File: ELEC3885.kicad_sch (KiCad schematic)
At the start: 4 parts

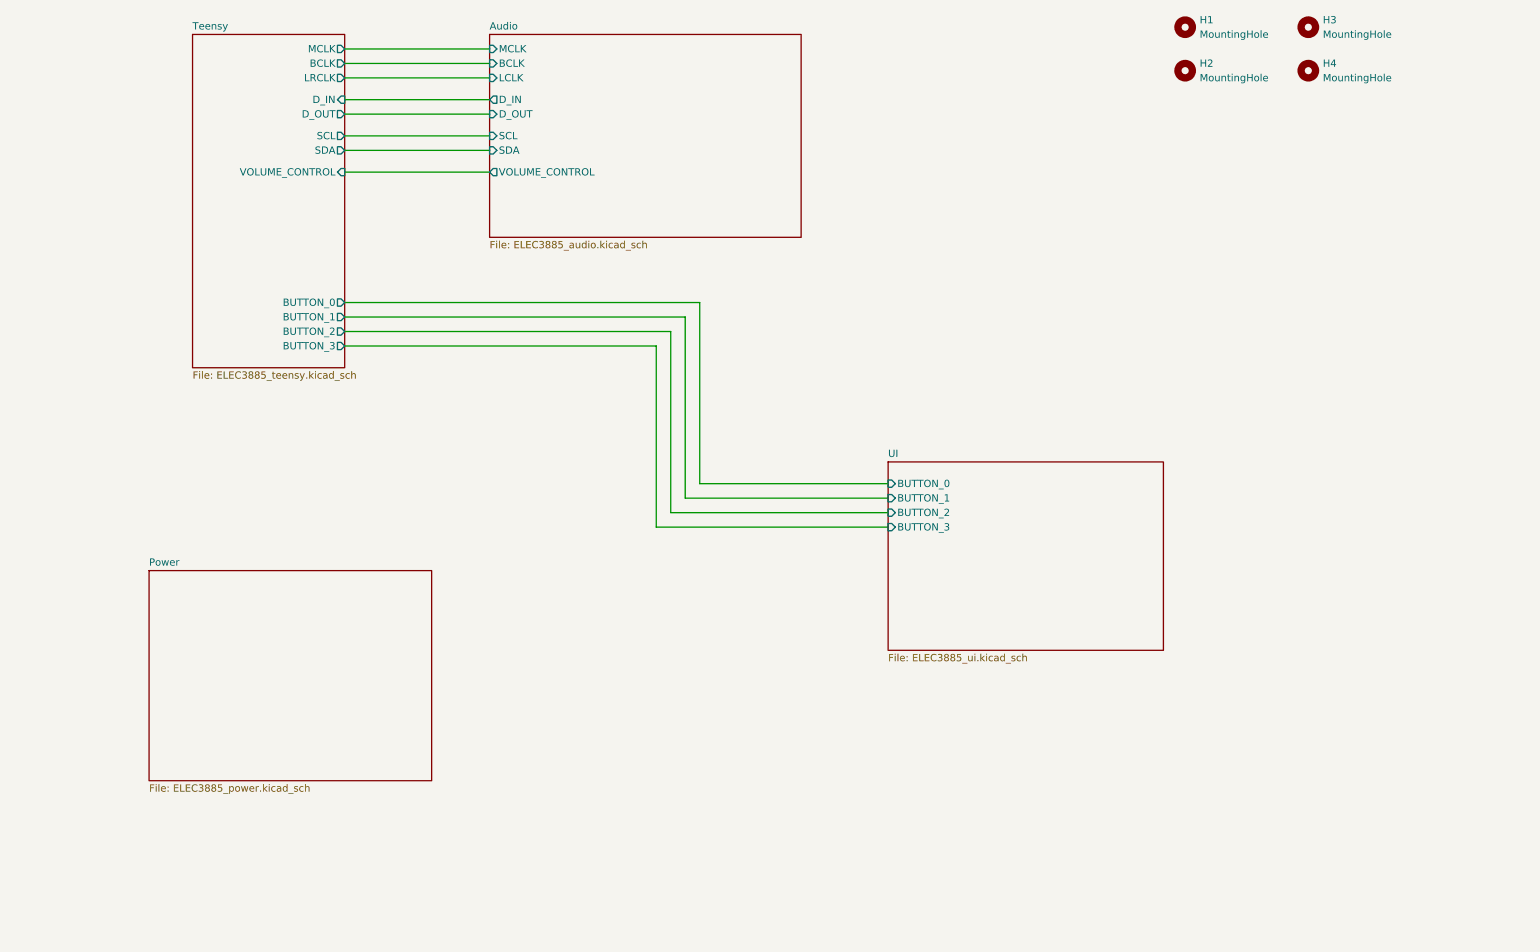
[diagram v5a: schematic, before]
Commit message: Fab cleanup, trace tapers added
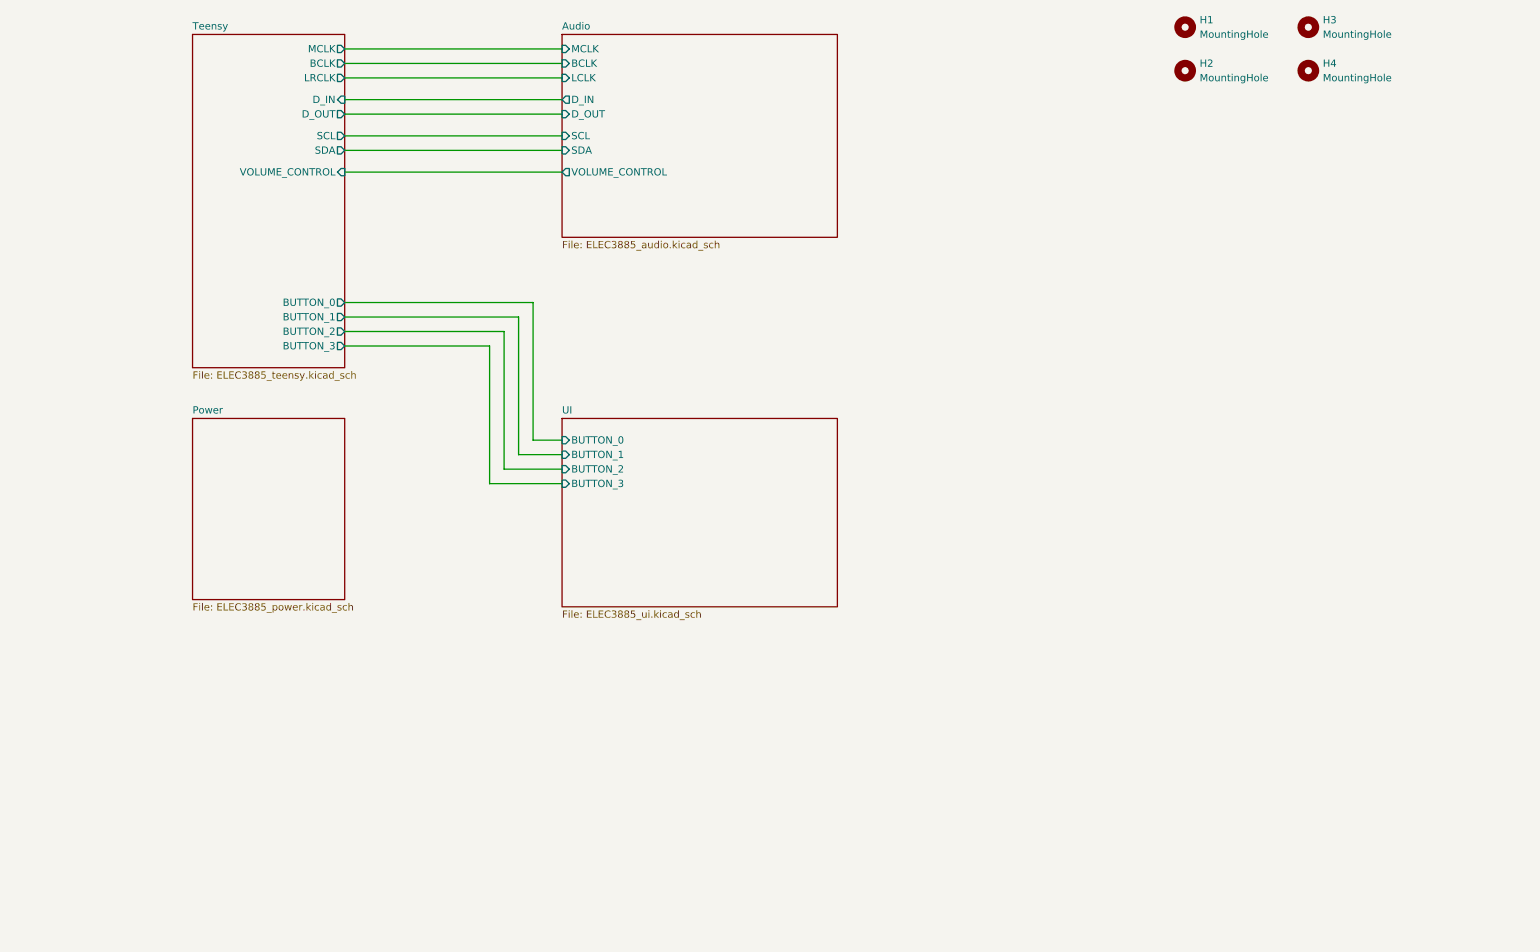
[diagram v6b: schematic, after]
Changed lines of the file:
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@@
 (kicad_sch (version 20211123) (generator eeschema)
   (paper "A4")
-  (wire (pts (xy 77.47 36.83) (xy 102.87 36.83))
-    (stroke (width 0) (type default) (color 0 0 0 0))
-  )
-  (wire (pts (xy 132.08 88.9) (xy 132.08 120.65))
-    (stroke (width 0) (type default) (color 0 0 0 0))
-  )
-  (wire (pts (xy 77.47 48.26) (xy 102.87 48.26))
-    (stroke (width 0) (type default) (color 0 0 0 0))
-  )
-  (wire (pts (xy 139.7 81.28) (xy 139.7 113.03))
-    (stroke (width 0) (type default) (color 0 0 0 0))
-  )
-  (wire (pts (xy 77.47 41.91) (xy 102.87 41.91))
-    (stroke (width 0) (type default) (color 0 0 0 0))
-  )
-  (wire (pts (xy 77.47 83.82) (xy 137.16 83.82))
-    (stroke (width 0) (type default) (color 0 0 0 0))
-  )
-  (wire (pts (xy 134.62 86.36) (xy 134.62 118.11))
-    (stroke (width 0) (type default) (color 0 0 0 0))
-  )
-  (wire (pts (xy 77.47 88.9) (xy 132.08 88.9))
-    (stroke (width 0) (type default) (color 0 0 0 0))
-  )
-  (wire (pts (xy 77.47 54.61) (xy 102.87 54.61))
-    (stroke (width 0) (type default) (color 0 0 0 0))
-  )
-  (wire (pts (xy 77.47 58.42) (xy 102.87 58.42))
-    (stroke (width 0) (type default) (color 0 0 0 0))
-  )
-  (wire (pts (xy 77.47 45.72) (xy 102.87 45.72))
-    (stroke (width 0) (type default) (color 0 0 0 0))
-  )
-  (wire (pts (xy 137.16 115.57) (xy 172.72 115.57))
-    (stroke (width 0) (type default) (color 0 0 0 0))
-  )
-  (wire (pts (xy 137.16 83.82) (xy 137.16 115.57))
-    (stroke (width 0) (type default) (color 0 0 0 0))
-  )
-  (wire (pts (xy 77.47 39.37) (xy 102.87 39.37))
-    (stroke (width 0) (type default) (color 0 0 0 0))
-  )
-  (wire (pts (xy 77.47 86.36) (xy 134.62 86.36))
-    (stroke (width 0) (type default) (color 0 0 0 0))
-  )
-  (wire (pts (xy 132.08 120.65) (xy 172.72 120.65))
-    (stroke (width 0) (type default) (color 0 0 0 0))
-  )
-  (wire (pts (xy 77.47 81.28) (xy 139.7 81.28))
-    (stroke (width 0) (type default) (color 0 0 0 0))
-  )
-  (wire (pts (xy 139.7 113.03) (xy 172.72 113.03))
-    (stroke (width 0) (type default) (color 0 0 0 0))
-  )
-  (wire (pts (xy 77.47 52.07) (xy 102.87 52.07))
-    (stroke (width 0) (type default) (color 0 0 0 0))
-  )
-  (wire (pts (xy 134.62 118.11) (xy 172.72 118.11))
+  (wire (pts (xy 77.47 36.83) (xy 115.57 36.83))
+    (stroke (width 0) (type default) (color 0 0 0 0))
+  )
+  (wire (pts (xy 115.57 105.41) (xy 110.49 105.41))
+    (stroke (width 0) (type default) (color 0 0 0 0))
+  )
+  (wire (pts (xy 105.41 110.49) (xy 105.41 86.36))
+    (stroke (width 0) (type default) (color 0 0 0 0))
+  )
+  (wire (pts (xy 77.47 48.26) (xy 115.57 48.26))
+    (stroke (width 0) (type default) (color 0 0 0 0))
+  )
+  (wire (pts (xy 77.47 41.91) (xy 115.57 41.91))
+    (stroke (width 0) (type default) (color 0 0 0 0))
+  )
+  (wire (pts (xy 77.47 83.82) (xy 107.95 83.82))
+    (stroke (width 0) (type default) (color 0 0 0 0))
+  )
+  (wire (pts (xy 77.47 88.9) (xy 102.87 88.9))
+    (stroke (width 0) (type default) (color 0 0 0 0))
+  )
+  (wire (pts (xy 115.57 107.95) (xy 107.95 107.95))
+    (stroke (width 0) (type default) (color 0 0 0 0))
+  )
+  (wire (pts (xy 77.47 54.61) (xy 115.57 54.61))
+    (stroke (width 0) (type default) (color 0 0 0 0))
+  )
+  (wire (pts (xy 77.47 58.42) (xy 115.57 58.42))
+    (stroke (width 0) (type default) (color 0 0 0 0))
+  )
+  (wire (pts (xy 115.57 113.03) (xy 102.87 113.03))
+    (stroke (width 0) (type default) (color 0 0 0 0))
+  )
+  (wire (pts (xy 115.57 110.49) (xy 105.41 110.49))
+    (stroke (width 0) (type default) (color 0 0 0 0))
+  )
+  (wire (pts (xy 77.47 45.72) (xy 115.57 45.72))
+    (stroke (width 0) (type default) (color 0 0 0 0))
+  )
+  (wire (pts (xy 102.87 113.03) (xy 102.87 88.9))
+    (stroke (width 0) (type default) (color 0 0 0 0))
+  )
+  (wire (pts (xy 77.47 39.37) (xy 115.57 39.37))
+    (stroke (width 0) (type default) (color 0 0 0 0))
+  )
+  (wire (pts (xy 107.95 83.82) (xy 107.95 107.95))
+    (stroke (width 0) (type default) (color 0 0 0 0))
+  )
+  (wire (pts (xy 77.47 86.36) (xy 105.41 86.36))
+    (stroke (width 0) (type default) (color 0 0 0 0))
+  )
+  (wire (pts (xy 77.47 81.28) (xy 110.49 81.28))
+    (stroke (width 0) (type default) (color 0 0 0 0))
+  )
+  (wire (pts (xy 110.49 105.41) (xy 110.49 81.28))
+    (stroke (width 0) (type default) (color 0 0 0 0))
+  )
+  (wire (pts (xy 77.47 52.07) (xy 115.57 52.07))
     (stroke (width 0) (type default) (color 0 0 0 0))
   )
@@
     )
   )
-  (sheet (at 172.72 109.22) (size 48.26 33.02) (fields_autoplaced)
+  (sheet (at 115.57 101.6) (size 48.26 33.02) (fields_autoplaced)
     (stroke (width 0.1524) (type solid) (color 0 0 0 0))
     (fill (color 0 0 0 0.0000))
-    (property "Sheet name" "UI" (id 0) (at 172.72 108.5084 0)
+    (property "Sheet name" "UI" (id 0) (at 115.57 100.8884 0)
       (effects (font (size 1.27 1.27)) (justify left bottom))
     )
-    (property "Sheet file" "ELEC3885_ui.kicad_sch" (id 1) (at 172.72 142.8246 0)
+    (property "Sheet file" "ELEC3885_ui.kicad_sch" (id 1) (at 115.57 135.2046 0)
       (effects (font (size 1.27 1.27)) (justify left top))
     )
-    (pin "BUTTON_3" input (at 172.72 120.65 180)
-      (effects (font (size 1.27 1.27)) (justify left))
-    )
-    (pin "BUTTON_0" input (at 172.72 113.03 180)
-      (effects (font (size 1.27 1.27)) (justify left))
-    )
-    (pin "BUTTON_2" input (at 172.72 118.11 180)
-      (effects (font (size 1.27 1.27)) (justify left))
-    )
-    (pin "BUTTON_1" input (at 172.72 115.57 180)
-      (effects (font (size 1.27 1.27)) (justify left))
-    )
-  )
-  (sheet (at 43.18 128.27) (size 49.53 36.83) (fields_autoplaced)
+    (pin "BUTTON_3" input (at 115.57 113.03 180)
+      (effects (font (size 1.27 1.27)) (justify left))
+    )
+    (pin "BUTTON_0" input (at 115.57 105.41 180)
+      (effects (font (size 1.27 1.27)) (justify left))
+    )
+    (pin "BUTTON_2" input (at 115.57 110.49 180)
+      (effects (font (size 1.27 1.27)) (justify left))
+    )
+    (pin "BUTTON_1" input (at 115.57 107.95 180)
+      (effects (font (size 1.27 1.27)) (justify left))
+    )
+  )
+  (sheet (at 50.8 101.6) (size 26.67 31.75) (fields_autoplaced)
     (stroke (width 0.1524) (type solid) (color 0 0 0 0))
     (fill (color 0 0 0 0.0000))
-    (property "Sheet name" "Power" (id 0) (at 43.18 127.5584 0)
+    (property "Sheet name" "Power" (id 0) (at 50.8 100.8884 0)
       (effects (font (size 1.27 1.27)) (justify left bottom))
     )
-    (property "Sheet file" "ELEC3885_power.kicad_sch" (id 1) (at 43.18 165.6846 0)
+    (property "Sheet file" "ELEC3885_power.kicad_sch" (id 1) (at 50.8 133.9346 0)
       (effects (font (size 1.27 1.27)) (justify left top))
     )
   )
-  (sheet (at 102.87 34.29) (size 54.61 35.56) (fields_autoplaced)
+  (sheet (at 115.57 34.29) (size 48.26 35.56) (fields_autoplaced)
     (stroke (width 0.1524) (type solid) (color 0 0 0 0))
     (fill (color 0 0 0 0.0000))
-    (property "Sheet name" "Audio" (id 0) (at 102.87 33.5784 0)
+    (property "Sheet name" "Audio" (id 0) (at 115.57 33.5784 0)
       (effects (font (size 1.27 1.27)) (justify left bottom))
     )
-    (property "Sheet file" "ELEC3885_audio.kicad_sch" (id 1) (at 102.87 70.4346 0)
+    (property "Sheet file" "ELEC3885_audio.kicad_sch" (id 1) (at 115.57 70.4346 0)
       (effects (font (size 1.27 1.27)) (justify left top))
     )
-    (pin "MCLK" input (at 102.87 36.83 180)
-      (effects (font (size 1.27 1.27)) (justify left))
-    )
-    (pin "BCLK" input (at 102.87 39.37 180)
-      (effects (font (size 1.27 1.27)) (justify left))
-    )
-    (pin "LCLK" input (at 102.87 41.91 180)
-      (effects (font (size 1.27 1.27)) (justify left))
-    )
-    (pin "D_IN" output (at 102.87 45.72 180)
-      (effects (font (size 1.27 1.27)) (justify left))
-    )
-    (pin "D_OUT" input (at 102.87 48.26 180)
-      (effects (font (size 1.27 1.27)) (justify left))
-    )
-    (pin "SCL" input (at 102.87 52.07 180)
-      (effects (font (size 1.27 1.27)) (justify left))
-    )
-    (pin "VOLUME_CONTROL" output (at 102.87 58.42 180)
-      (effects (font (size 1.27 1.27)) (justify left))
-    )
-    (pin "SDA" input (at 102.87 54.61 180)
+    (pin "MCLK" input (at 115.57 36.83 180)
+      (effects (font (size 1.27 1.27)) (justify left))
+    )
+    (pin "BCLK" input (at 115.57 39.37 180)
+      (effects (font (size 1.27 1.27)) (justify left))
+    )
+    (pin "LCLK" input (at 115.57 41.91 180)
+      (effects (font (size 1.27 1.27)) (justify left))
+    )
+    (pin "D_IN" output (at 115.57 45.72 180)
+      (effects (font (size 1.27 1.27)) (justify left))
+    )
+    (pin "D_OUT" input (at 115.57 48.26 180)
+      (effects (font (size 1.27 1.27)) (justify left))
+    )
+    (pin "SCL" input (at 115.57 52.07 180)
+      (effects (font (size 1.27 1.27)) (justify left))
+    )
+    (pin "VOLUME_CONTROL" output (at 115.57 58.42 180)
+      (effects (font (size 1.27 1.27)) (justify left))
+    )
+    (pin "SDA" input (at 115.57 54.61 180)
       (effects (font (size 1.27 1.27)) (justify left))
     )
@@
     )
     (path "/ffd175d1-912a-4224-be1e-a8198680f46b/4263fe08-e8ff-4963-bba5-a04dc0cf743a"
-      (reference "FB1") (unit 1) (value "FerriteBead") (footprint "Inductor_SMD:L_0603_1608Metric")
+      (reference "FB1") (unit 1) (value "600") (footprint "Inductor_SMD:L_0603_1608Metric")
     )
     (path "/fcca16c4-ef75-486f-ac64-d731431c8750"
